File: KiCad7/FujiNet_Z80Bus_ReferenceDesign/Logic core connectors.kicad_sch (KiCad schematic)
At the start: 1 part

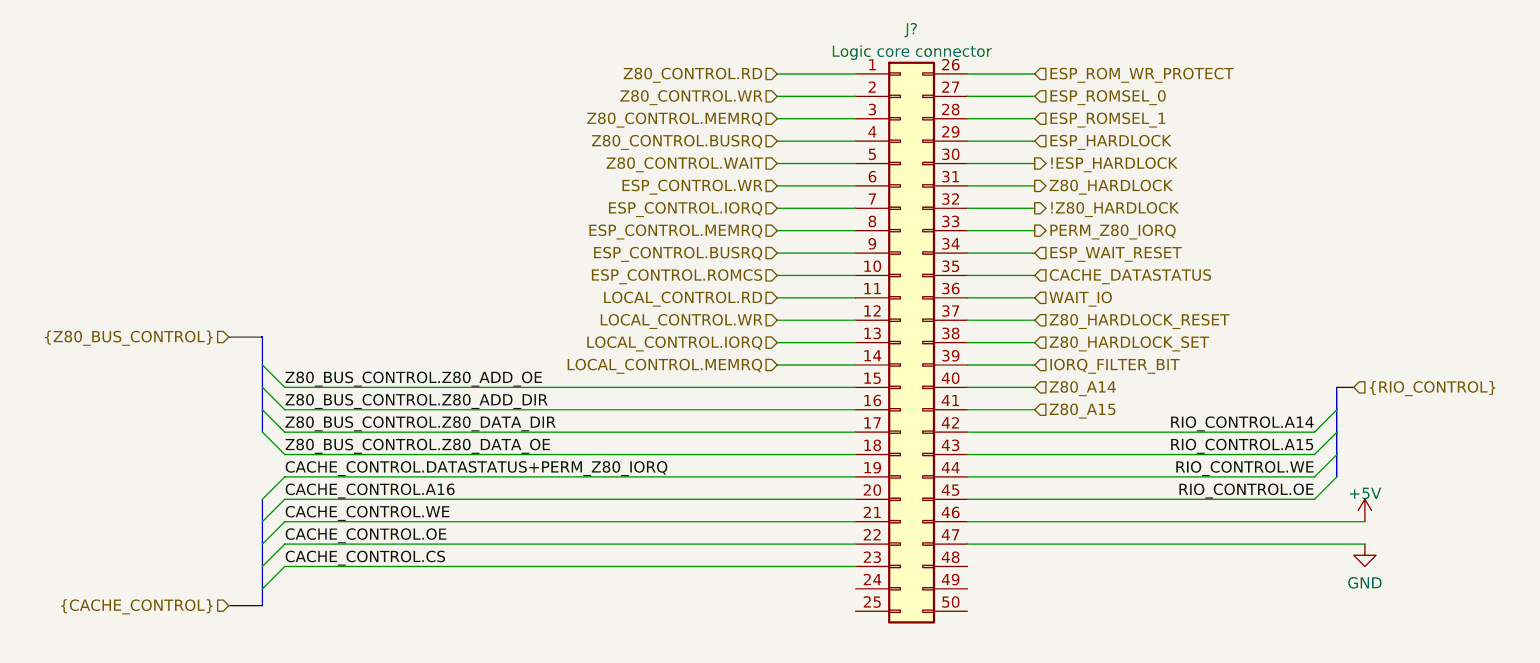
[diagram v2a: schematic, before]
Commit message: KiCAD - grid alignment errors fixed
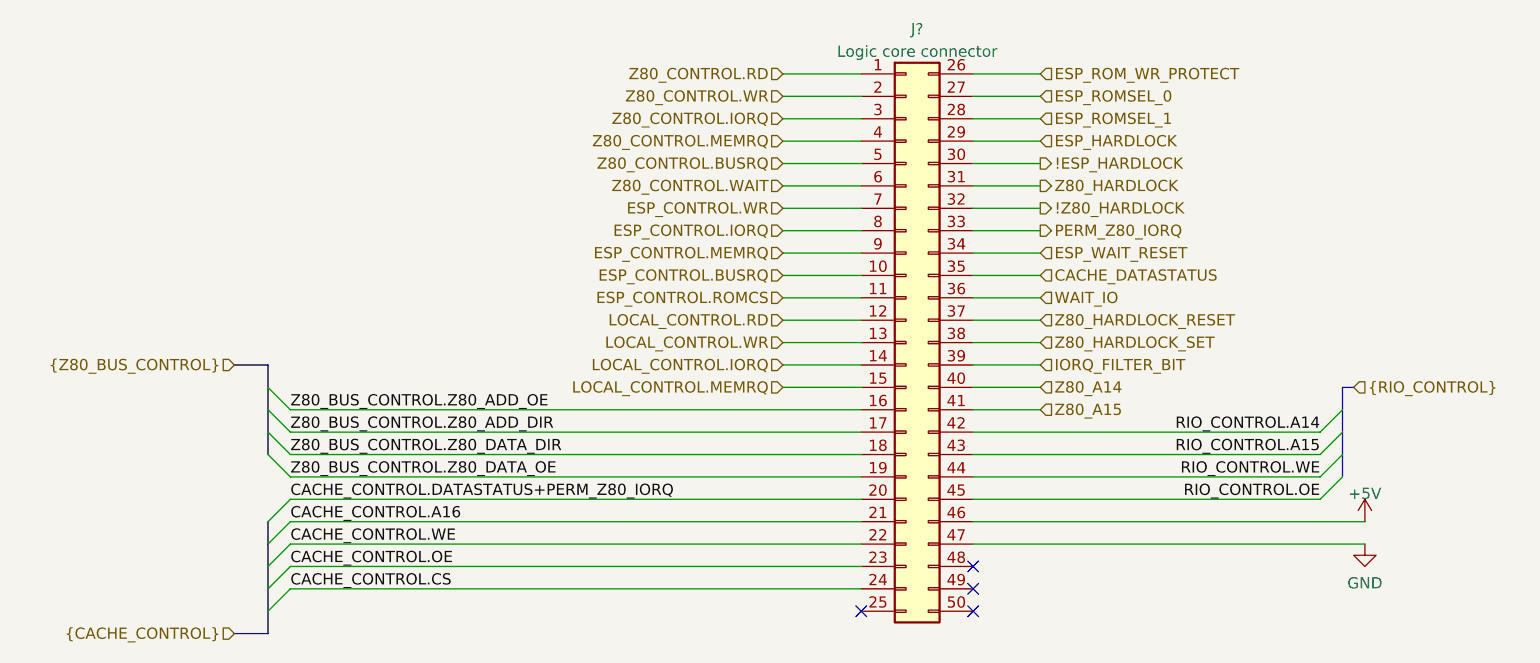
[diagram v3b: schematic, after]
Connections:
- net CACHE_CONTROL.A16: now also J?.21 (Pin_21); no longer J?.20 (Pin_20)
- net CACHE_CONTROL.CS: now also J?.24 (Pin_24); no longer J?.23 (Pin_23)
- net CACHE_CONTROL.DATASTATUS+PERM_Z80_IORQ: now also J?.20 (Pin_20); no longer J?.19 (Pin_19)
- net CACHE_CONTROL.OE: now also J?.23 (Pin_23); no longer J?.22 (Pin_22)
- net CACHE_CONTROL.WE: now also J?.22 (Pin_22); no longer J?.21 (Pin_21)
- net ESP_CONTROL.BUSRQ: now also J?.10 (Pin_10); no longer J?.9 (Pin_9)
- net ESP_CONTROL.IORQ: now also J?.8 (Pin_8); no longer J?.7 (Pin_7)
- net ESP_CONTROL.MEMRQ: now also J?.9 (Pin_9); no longer J?.8 (Pin_8)
- net ESP_CONTROL.ROMCS: now also J?.11 (Pin_11); no longer J?.10 (Pin_10)
- net ESP_CONTROL.WR: now also J?.7 (Pin_7); no longer J?.6 (Pin_6)
- net LOCAL_CONTROL.IORQ: now also J?.14 (Pin_14); no longer J?.13 (Pin_13)
- net LOCAL_CONTROL.MEMRQ: now also J?.15 (Pin_15); no longer J?.14 (Pin_14)
- net LOCAL_CONTROL.RD: now also J?.12 (Pin_12); no longer J?.11 (Pin_11)
- net LOCAL_CONTROL.WR: now also J?.13 (Pin_13); no longer J?.12 (Pin_12)
- net Z80_BUS_CONTROL.Z80_ADD_DIR: now also J?.17 (Pin_17); no longer J?.16 (Pin_16)
- net Z80_BUS_CONTROL.Z80_ADD_OE: now also J?.16 (Pin_16); no longer J?.15 (Pin_15)
- net Z80_BUS_CONTROL.Z80_DATA_DIR: now also J?.18 (Pin_18); no longer J?.17 (Pin_17)
- net Z80_BUS_CONTROL.Z80_DATA_OE: now also J?.19 (Pin_19); no longer J?.18 (Pin_18)
- net Z80_CONTROL.BUSRQ: now also J?.5 (Pin_5); no longer J?.4 (Pin_4)
- net Z80_CONTROL.MEMRQ: now also J?.4 (Pin_4); no longer J?.3 (Pin_3)
- net Z80_CONTROL.WAIT: now also J?.6 (Pin_6); no longer J?.5 (Pin_5)
- new net Z80_CONTROL.IORQ: J?.3 (Pin_3)
- no-connect marks 0 -> 4
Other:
- moved on the sheet: J?
